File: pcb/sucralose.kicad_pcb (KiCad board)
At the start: 2 copper layers, 155.3 x 89.9 mm, 95 parts, among them M1 MountingHole_1.2mm_M1

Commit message: M1 hole 2.0 mm below the last nice!view pad (pad 1 MOSI/CS at 102.101,68.435), on the header line: (102.414, 70.41). 0.52 mm web to the pad ring; nearest copper ROW0 B.Cu 1.08 mm. DRC count unchanged (361).
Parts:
- added M1: MountingHole_1.2mm_M1, CustomParts:MountingHole_1.2mm_M1, F.Cu at (102.4, 70.4)
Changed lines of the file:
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@@
 		)
+	)
+(footprint "CustomParts:MountingHole_1.2mm_M1"
+		(layer "F.Cu")
+		(at 102.414 70.41)
+		(descr "Mounting Hole 1.2mm, M1, no annular. Courtyard and head outline 2.2 mm dia (ISO 7045 / JIS B 1111 M1-M1.2 pan head dk max 2.0)")
+		(tags "mountinghole M2")
+		(property "Reference" "M1"
+			(at 2.523779 0.090644 0)
+			(layer "F.SilkS")
+			(effects
+				(font
+					(size 1 1)
+					(thickness 0.15)
+				)
+			)
+		)
+		(property "Value" "MountingHole_1.2mm_M1"
+			(at 0 3.15 0)
+			(layer "F.Fab")
+			(hide yes)
+			(effects
+				(font
+					(size 1 1)
+					(thickness 0.15)
+				)
+			)
+		)
+		(property "Datasheet" ""
+			(at 0 0 0)
+			(layer "F.Fab")
+			(hide yes)
+			(effects
+				(font
+					(size 1.27 1.27)
+				)
+			)
+		)
+		(property "Description" ""
+			(at 0 0 0)
+			(layer "F.Fab")
+			(hide yes)
+			(effects
+				(font
+					(size 1.27 1.27)
+				)
+			)
+		)
+		(property "KiLib_Generator" "mounting_hardware/mounting_hole"
+			(at 0 0 0)
+			(layer "F.SilkS")
+			(hide yes)
+			(effects
+				(font
+					(size 1 1)
+					(thickness 0.15)
+				)
+			)
+		)
+		(attr exclude_from_pos_files exclude_from_bom)
+		(duplicate_pad_numbers_are_jumpers no)
+		(fp_circle
+			(center 0 0)
+			(end 1.1 0)
+			(stroke
+				(width 0.05)
+				(type solid)
+			)
+			(fill no)
+			(layer "Cmts.User")
+		)
+		(fp_circle
+			(center 0 0)
+			(end 1.1 0)
+			(stroke
+				(width 0.05)
+				(type solid)
+			)
+			(fill no)
+			(layer "F.CrtYd")
+		)
+		(fp_text user "${REFERENCE}"
+			(at 0 0 0)
+			(layer "F.Fab")
+			(effects
+				(font
+					(size 1 1)
+					(thickness 0.15)
+				)
+			)
+		)
+		(pad "" np_thru_hole circle
+			(at 0 0)
+			(size 1.2 1.2)
+			(drill 1.2)
+			(layers "*.Cu" "*.Mask")
+		)
+		(embedded_fonts no)
 	)
 	(footprint "sucralose:MouseBite_0.6mm_col7"

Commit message: Display M1 hole moved to 5.0 mm (c-c) below the last nice!view pad, on the header line: (102.8825, 73.374). ROW0 B.Cu diagonal that crossed it rerouted (45-H-45 dogleg, 0.35+ mm clearance). DRC count unchanged (361).
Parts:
- moved M1 3.00 mm to (102.9, 73.4)
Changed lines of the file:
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@@
 (footprint "CustomParts:MountingHole_1.2mm_M1"
 		(layer "F.Cu")
-		(at 102.414 70.41)
+		(at 102.8825 73.374)
 		(descr "Mounting Hole 1.2mm, M1, no annular. Courtyard and head outline 2.2 mm dia (ISO 7045 / JIS B 1111 M1-M1.2 pan head dk max 2.0)")
 		(tags "mountinghole M2")
@@
 	)
 	(segment
+		(start 106.7523 68.625)
+		(end 104.0023 71.375)
+		(width 0.25)
+		(layer "B.Cu")
+		(net "ROW0")
+	)
+	(segment
+		(start 104.0023 71.375)
+		(end 98.7523 71.375)
+		(width 0.25)
+		(layer "B.Cu")
+		(net "ROW0")
+	)
+	(segment
+		(start 98.7523 71.375)
+		(end 94.6273 75.5)
+		(width 0.25)
+		(layer "B.Cu")
+		(net "ROW0")
+	)
+	(segment
+		(start 94.6273 75.5)
+		(end 94.3773 75.5)
+		(width 0.25)
+		(layer "B.Cu")
+		(net "ROW0")
+	)
+	(segment
 		(start 165.6273 65)
 		(end 166 65.3)
@@
 	)
 	(segment
-		(start 106.7523 68.6250)
-		(end 99.8773 75.5000)
-		(width 0.25)
-		(layer "B.Cu")
-		(net "ROW0")
-		(uuid "ryn1000b-b528-4ecb-bf91-e8fdf6734b84")
-	)
-	(segment
-		(start 99.8773 75.5000)
-		(end 94.3773 75.5000)
-		(width 0.25)
-		(layer "B.Cu")
-		(net "ROW0")
-		(uuid "ryn1cc56-ea92-4946-9a0b-04ea6cdb8184")
-	)
-	(segment

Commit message: Display M1 hole moved to 3.5 mm (c-c) below the last nice!view pad, on the header line: (102.648, 71.892). ROW0 B.Cu diagonal rerouted as 45-H-45 above the hole (clearance >=0.53 mm). DRC count unchanged (361).
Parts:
- moved M1 1.50 mm to (102.6, 71.9)
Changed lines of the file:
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@@
 (footprint "CustomParts:MountingHole_1.2mm_M1"
 		(layer "F.Cu")
-		(at 102.8825 73.374)
+		(at 102.648 71.892)
 		(descr "Mounting Hole 1.2mm, M1, no annular. Courtyard and head outline 2.2 mm dia (ISO 7045 / JIS B 1111 M1-M1.2 pan head dk max 2.0)")
 		(tags "mountinghole M2")
@@
 	(segment
 		(start 106.7523 68.625)
-		(end 104.0023 71.375)
+		(end 105.0023 70.375)
 		(width 0.25)
 		(layer "B.Cu")
@@
 	)
 	(segment
-		(start 104.0023 71.375)
-		(end 98.7523 71.375)
+		(start 105.0023 70.375)
+		(end 99.5023 70.375)
 		(width 0.25)
 		(layer "B.Cu")
@@
 	)
 	(segment
-		(start 98.7523 71.375)
-		(end 94.6273 75.5)
-		(width 0.25)
-		(layer "B.Cu")
-		(net "ROW0")
-	)
-	(segment
-		(start 94.6273 75.5)
+		(start 99.5023 70.375)
 		(end 94.3773 75.5)
 		(width 0.25)

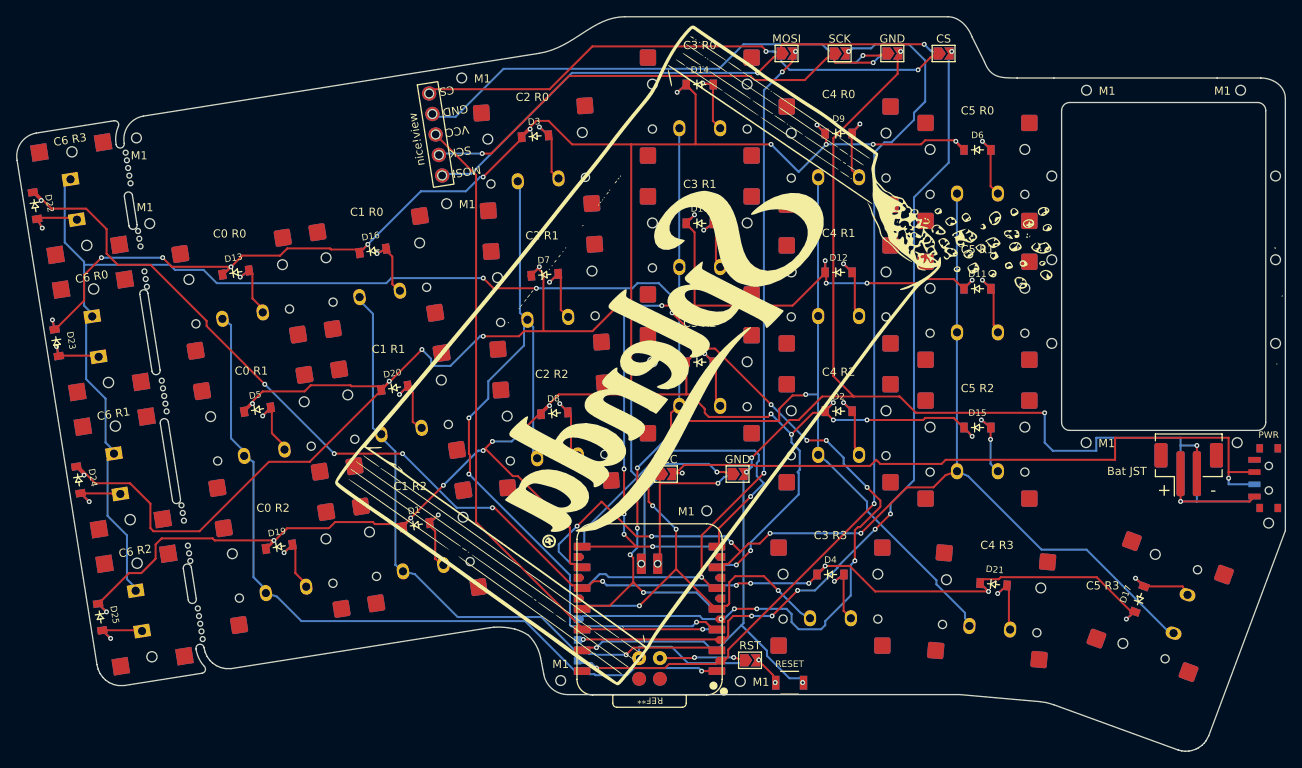
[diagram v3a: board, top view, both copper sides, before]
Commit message: Moved top, right M1 hole above battery bay.
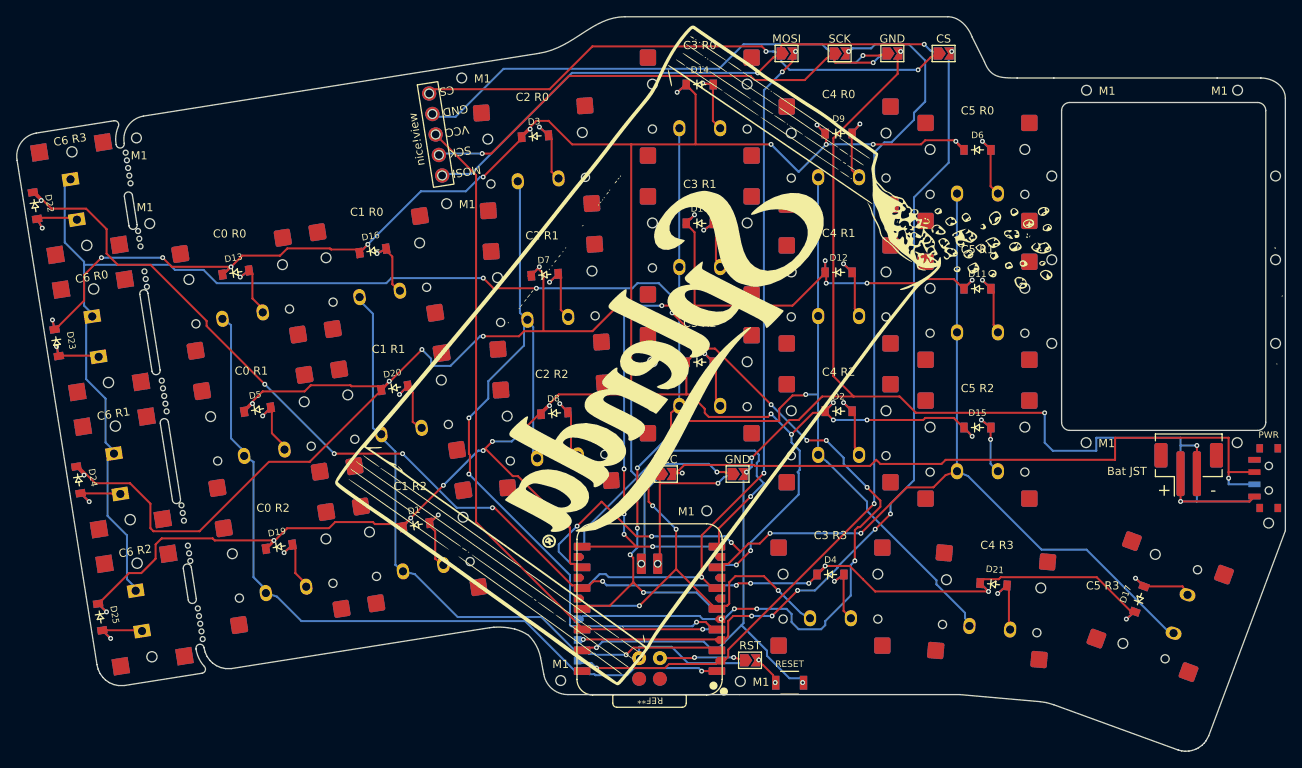
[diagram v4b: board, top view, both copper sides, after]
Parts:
- moved M1 0.37 mm to (199.5, 58.0)

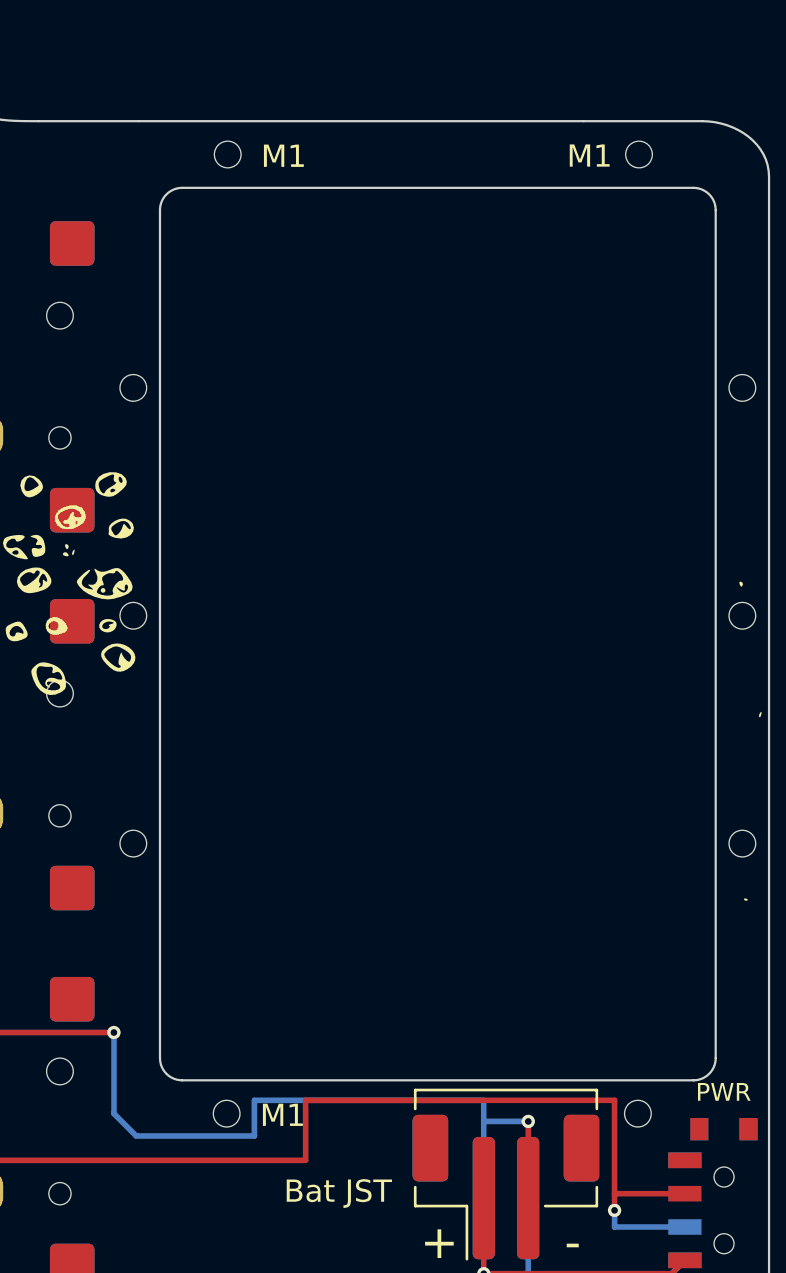
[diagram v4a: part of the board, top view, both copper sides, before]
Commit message: Battery-bay M1 holes symmetric about the cutout (177.95-202.95 x 59.5-99.65, centre 190.45,79.575): (181.45,58) (199.45,58) (181.45,101.15) (199.45,101.15); 9.0 mm off centre in X, 21.575 mm in Y. GND B.Cu dogleg nudged 182.2->182.5 to clear the moved bottom-left hole. Silk: BATTERY BAY 25x40.15mm (measured from Edge.Cuts). DRC violation set unchanged (361).
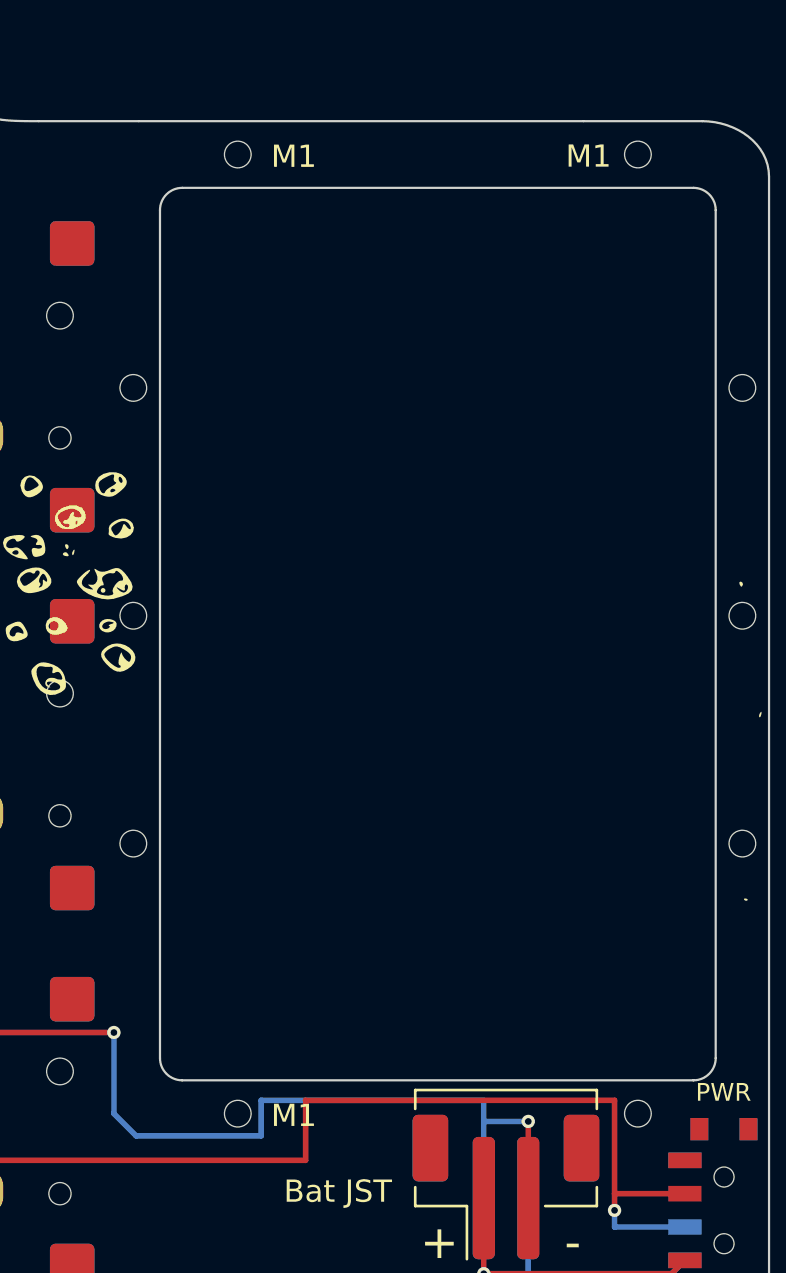
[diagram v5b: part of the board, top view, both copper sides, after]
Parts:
- moved M1 0.50 mm to (181.4, 101.2)
- moved M1 0.45 mm to (181.4, 58.0)
- moved M1 0.05 mm to (199.4, 58.0)
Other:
- board text added: "BATTERY BAY 25x40.15mm"
- board text removed: "BATTERY BAY 25x38.5mm"
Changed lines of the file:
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@@
 	(footprint "CustomParts:MountingHole_1.2mm_M1"
 		(layer "F.Cu")
-		(at 180.95 101.15)
+		(at 181.45 101.15)
 		(descr "Mounting Hole 1.2mm, M1, no annular. Courtyard and head outline 2.2 mm dia (ISO 7045 / JIS B 1111 M1-M1.2 pan head dk max 2.0)")
 		(tags "mountinghole M2")
@@
 	(footprint "CustomParts:MountingHole_1.2mm_M1"
 		(layer "F.Cu")
-		(at 199.5 58)
+		(at 199.45 58)
 		(descr "Mounting Hole 1.2mm, M1, no annular. Courtyard and head outline 2.2 mm dia (ISO 7045 / JIS B 1111 M1-M1.2 pan head dk max 2.0)")
 		(tags "mountinghole M2")
@@
 	(footprint "CustomParts:MountingHole_1.2mm_M1"
 		(layer "F.Cu")
-		(at 180.996793 58)
+		(at 181.45 58)
 		(descr "Mounting Hole 1.2mm, M1, no annular. Courtyard and head outline 2.2 mm dia (ISO 7045 / JIS B 1111 M1-M1.2 pan head dk max 2.0)")
 		(tags "mountinghole M2")
@@
 		)
 	)
-	(gr_text "BATTERY BAY 25x38.5mm"
+	(gr_text "BATTERY BAY 25x40.15mm"
 		(at 188.5 78.75 270)
 		(layer "Dwgs.User")
@@
 	)
 	(segment
-		(start 182.2 102.15)
-		(end 182.2 100.55)
+		(start 182.5 102.15)
+		(end 182.5 100.55)
 		(width 0.25)
 		(layer "B.Cu")
@@
 	(segment
 		(start 176.8773 102.15)
-		(end 182.2 102.15)
+		(end 182.5 102.15)
 		(width 0.25)
 		(layer "B.Cu")
@@
 	)
 	(segment
-		(start 182.2 100.55)
+		(start 182.5 100.55)
 		(end 192.514117 100.55)
 		(width 0.25)

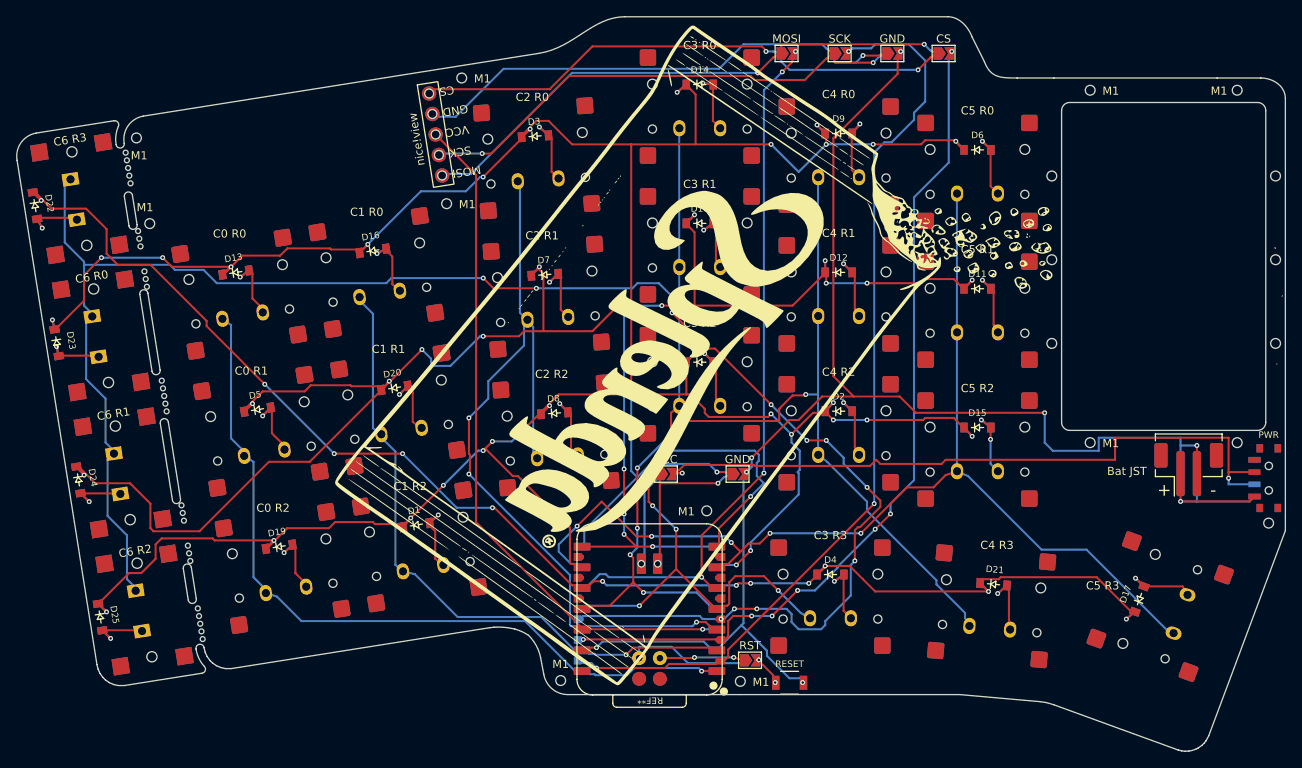
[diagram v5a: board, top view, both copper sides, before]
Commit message: Display inboard 2.8 mm along the column-0 top edge (with its top and two left M1 holes); header M1 at (102.648,71.892) left in place. Main left edge and pinky-col7 strip (switches, diodes, mouse bites, slot, Edge.Cuts) moved inboard 2.4 mm: edge u 52.30 -> 54.70, 0.62 mm from C0 keycap outline. Display stubs DISP_H1/H4/VCC re-joined; COL6/ROW0-3 bridge crossings re-routed; stale ROW3 detour removed. DRC 361, same categories and same 7 unconnected pads as before.
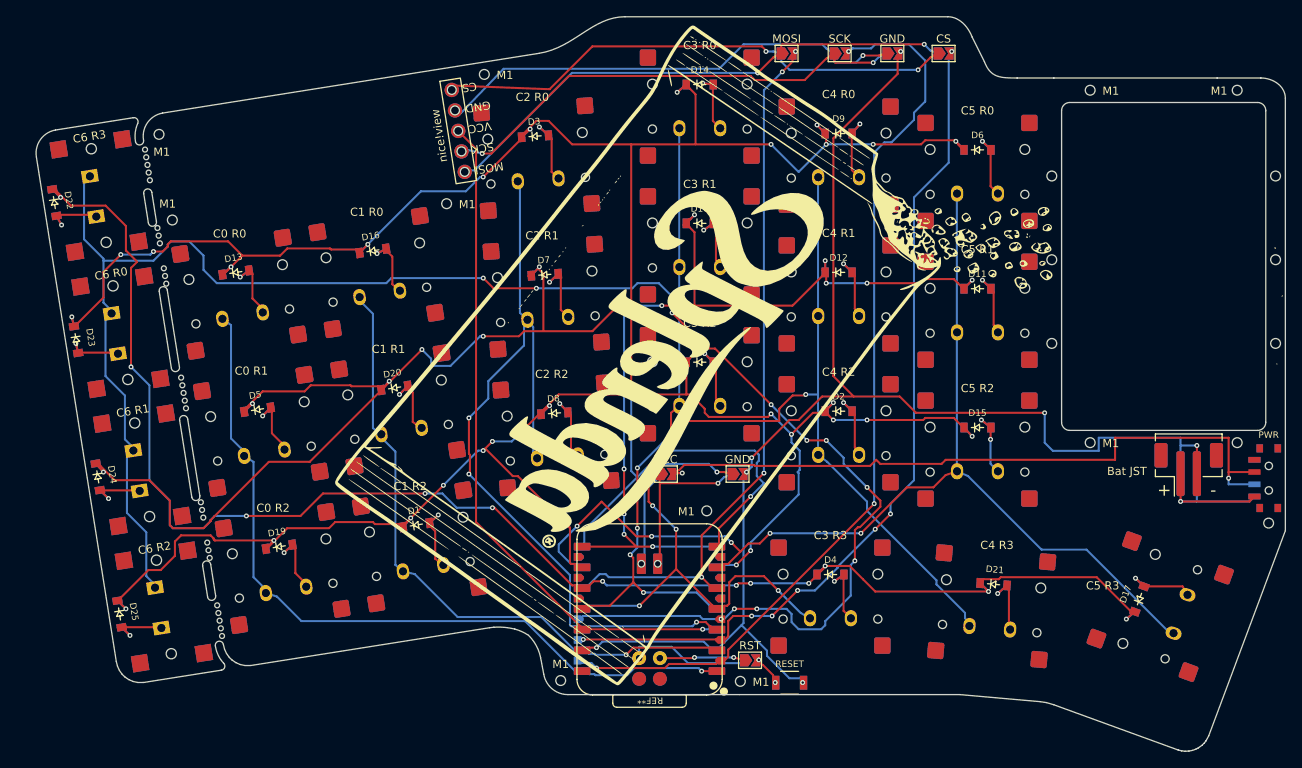
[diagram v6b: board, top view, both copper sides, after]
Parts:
- moved M1 2.80 mm to (69.1, 73.9)
- moved M1 2.80 mm to (67.4, 63.4)
- moved M1 2.80 mm to (107.3, 56.1)
- moved display* 2.80 mm to (87.8, 65.6) (x2)
- moved C6 R1 2.40 mm to (65.4, 104.5)
- moved C6 R2 2.40 mm to (68.0, 121.3)
- moved D23 2.40 mm to (57.3, 88.5)
- moved D24 2.40 mm to (59.9, 105.3)
- moved MB3 2.40 mm to (73.1, 111.9)
- moved MB4 2.40 mm to (74.9, 122.9)
- moved MB5 2.40 mm to (70.4, 95.1)
- moved C6 R0 2.40 mm to (62.7, 87.7)
- moved C6 R3 2.40 mm to (60.1, 70.9)
- moved D22 2.40 mm to (54.6, 71.8)
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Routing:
- net ROW3: track 175.0 -> 193.1 mm
- net DISP_H1: track 67.3 -> 64.3 mm
- net DISP_H4: track 60.3 -> 57.4 mm
- net DISP_H5: track 66.3 -> 63.5 mm
- net DISP_H2: track 60.8 -> 58.1 mm
- net ROW1: track 238.3 -> 235.9 mm
- net ROW2: track 191.9 -> 189.8 mm
- net COL6: track 218.6 -> 219.6 mm
- net VCC: track 83.7 -> 83.0 mm
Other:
- board size 155.3 x 89.9 mm -> 153 x 89.9 mm
